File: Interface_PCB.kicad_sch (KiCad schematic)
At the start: 40 parts, among them IC1 STM32L412RBT6P, J1 USB_B, J2 AVR-JTAG-10, J3 Conn_01x04, J4 Conn_01x04, J5 Conn_01x04, J6 Conn_01x04, J7 Micro_SD_Card, U1 AMS1117-3.3, Y1 Crystal, Y2 Crystal

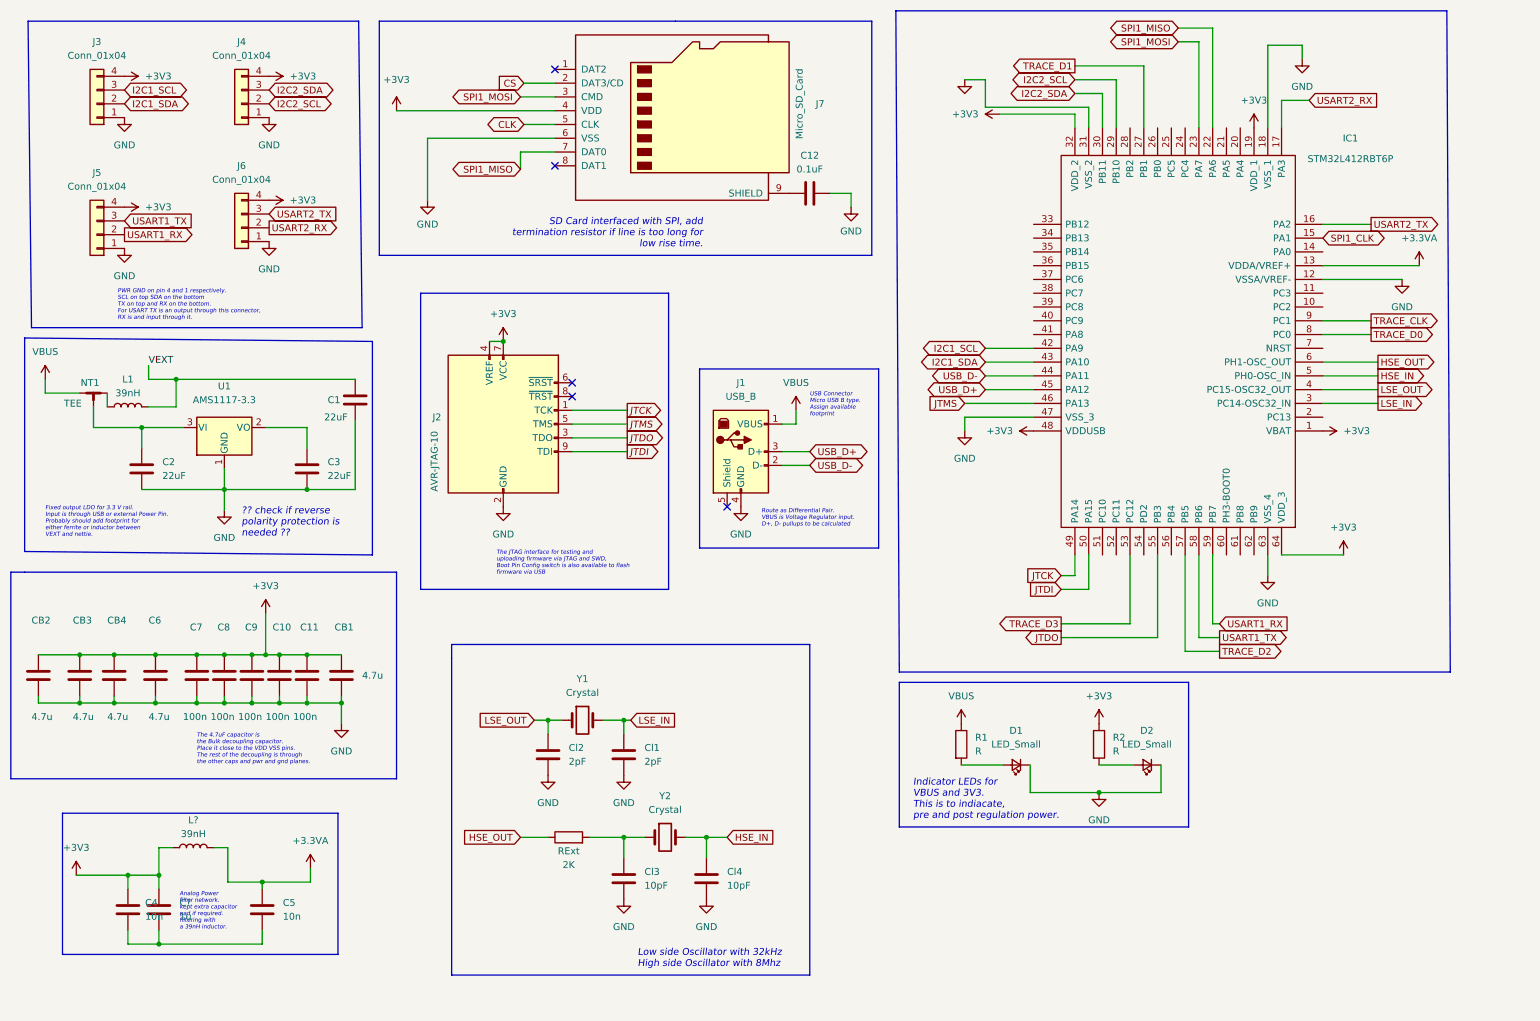
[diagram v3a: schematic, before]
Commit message: Components are on PCB doc, Stackup and Layout to be done, verify footprints
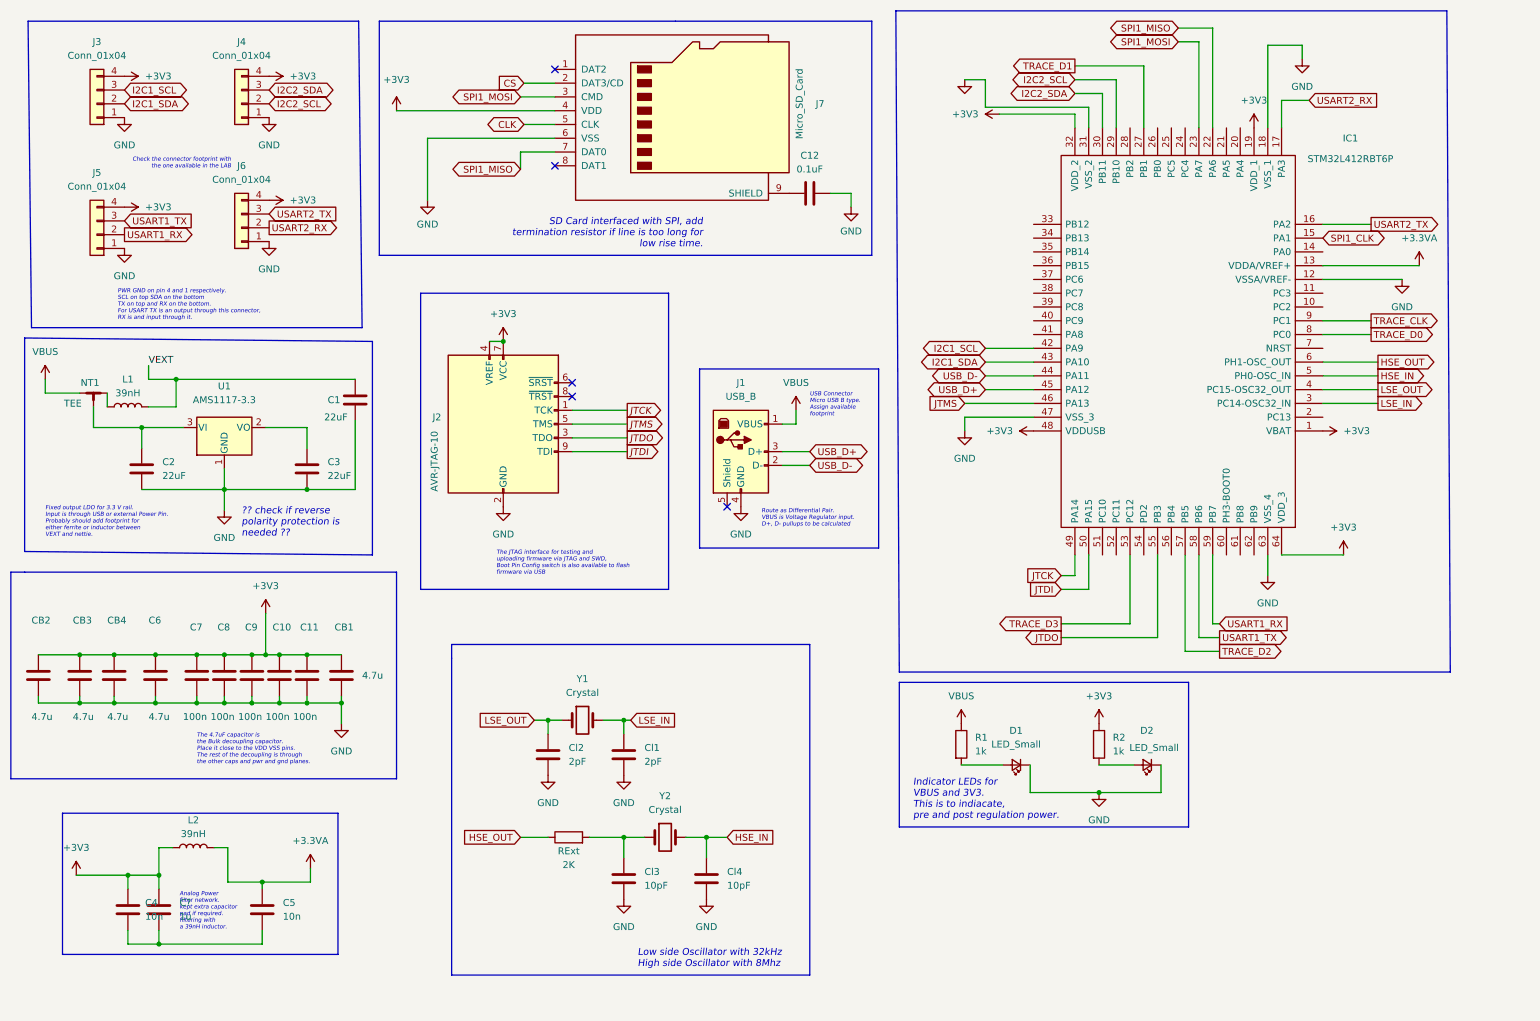
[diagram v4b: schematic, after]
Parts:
- C1, C10, C11, C2, C3, C4, C5, C7, C8, C9, C?: footprint (none) -> Capacitor_SMD:C_0603_1608Metric
- C6, CB1, CB2, CB3, CB4: footprint (none) -> Capacitor_SMD:C_0805_2012Metric
- Cl1, Cl2, Cl3, Cl4: footprint (none) -> Capacitor_SMD:C_0402_1005Metric
- D1, D2: footprint (none) -> LED_SMD:LED_0603_1608Metric
- J2: footprint (none) -> Connector_PinHeader_2.54mm:PinHeader_2x05_P2.54mm_Vertical_SMD
- J4, J5, J6: footprint (none) -> Connector_Molex:Molex_CLIK-Mate_502382-0270_1x02-1MP_P1.25mm_Vertical
- L2: renamed from L?; footprint (none) -> Capacitor_SMD:C_0603_1608Metric
- R1, R2: value R -> 1k; footprint (none) -> Resistor_SMD:R_0603_1608Metric
- RExt: footprint (none) -> Resistor_SMD:R_0603_1608Metric
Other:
- note added: "Check the connector footprint with the one available in the LAB"

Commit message: Added all component links and modified the footprints
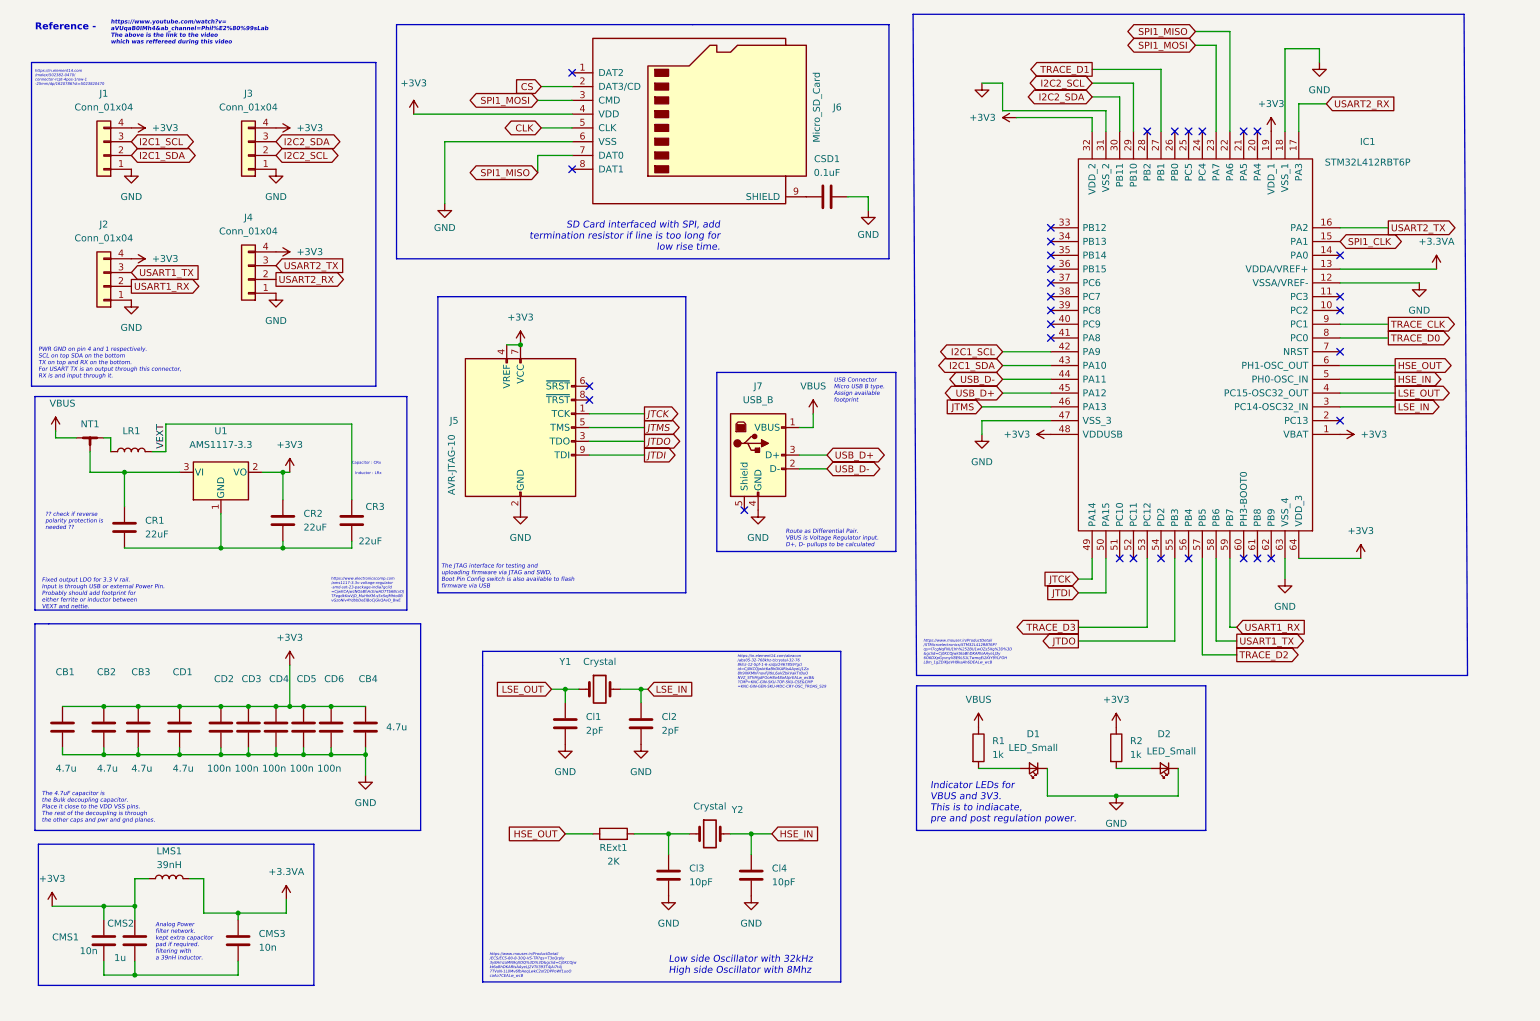
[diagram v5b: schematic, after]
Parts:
- removed C1, C2, C3: 22uF, Capacitor_SMD:C_0603_1608Metric, symbol Device:C
- removed C10, C11, C7, C8, C9: 100n, Capacitor_SMD:C_0603_1608Metric, symbol Device:C
- removed C12: 0.1uF, symbol Device:C
- removed C4, C5: 10n, Capacitor_SMD:C_0603_1608Metric, symbol Device:C
- removed C6: 4.7u, Capacitor_SMD:C_0805_2012Metric, symbol Device:C
- removed C?: 1u, Capacitor_SMD:C_0603_1608Metric, symbol Device:C
- removed J1: USB_B, Connector_USB:USB_Micro-B_Amphenol_10104110_Horizontal, symbol Connector:USB_B
- removed J2: AVR-JTAG-10, Connector_PinHeader_2.54mm:PinHeader_2x05_P2.54mm_Vertical_SMD, symbol Connector:AVR-JTAG-10
- removed J5, J6: Conn_01x04, Connector_Molex:Molex_CLIK-Mate_502382-0270_1x02-1MP_P1.25mm_Vertical, symbol Connector_Generic:Conn_01x04
- removed J7: Micro_SD_Card, Connector_Card:microSD_HC_Wuerth_693072010801, symbol Connector:Micro_SD_Card
- removed L1: 39nH, symbol Device:L
- removed L2: 39nH, Capacitor_SMD:C_0603_1608Metric, symbol Device:L
- removed RExt: 2K, Resistor_SMD:R_0603_1608Metric, symbol Device:R
- added CD1: 4.7u, Capacitor_SMD:C_0805_2012Metric, symbol Device:C
- added CD2, CD3, CD4, CD5, CD6: 100n, Capacitor_SMD:C_0603_1608Metric, symbol Device:C
- added CMS1, CMS3: 10n, Capacitor_SMD:C_0603_1608Metric, symbol Device:C
- added CMS2: 1u, Capacitor_SMD:C_0603_1608Metric, symbol Device:C
- added CR1, CR2, CR3: 22uF, Capacitor_SMD:C_0402_1005Metric, symbol Device:C
- added CSD1: 0.1uF, Capacitor_SMD:C_0402_1005Metric, symbol Device:C
- added J1, J2: Conn_01x04, Connector_Molex:Molex_CLIK-Mate_502382-0470_1x04-1MP_P1.25mm_Vertical, symbol Connector_Generic:Conn_01x04
- added J5: AVR-JTAG-10, Connector_PinHeader_2.54mm:PinHeader_2x05_P2.54mm_Vertical_SMD, symbol Connector:AVR-JTAG-10
- added J6: Micro_SD_Card, SamacSys_Parts:693072010801, symbol Connector:Micro_SD_Card
- added J7: USB_B, Connector_USB1:USB_Micro-B_Amphenol_10104110_Horizontal, symbol Connector:USB_B
- added LMS1: 39nH, Capacitor_SMD:C_0603_1608Metric, symbol Device:L
- added LR1: 39nH, Inductor_SMD:L_0402_1005Metric, symbol Device:L
- added RExt1: 2K, Resistor_SMD:R_0603_1608Metric, symbol Device:R
- J3: footprint (none) -> Connector_Molex:Molex_CLIK-Mate_502382-0470_1x04-1MP_P1.25mm_Vertical
- J4: footprint Connector_Molex:Molex_CLIK-Mate_502382-0270_1x02-1MP_P1.25mm_Vertical -> Connector_Molex:Molex_CLIK-Mate_502382-0470_1x04-1MP_P1.25mm_Vertical
- NT1: value TEE -> NetTie_3_Tee; footprint (none) -> NetTie:NetTie-3_SMD_Pad2.0mm
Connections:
- net +3.3VA: now also CMS3.1, LMS1.2
- net +3V3: now also U1.2 (VO), CD1.1, CD2.1, CD3.1, CD4.1, CD5.1, CD6.1, CMS1.1, CMS2.1, CR2.1, J1.4 (Pin_4), J2.4 (Pin_4), J5.4 (VREF), J5.7 (VCC), J6.4 (VDD), LMS1.1
- net CLK: now also J6.5 (CLK)
- net CS: now also J6.2 (DAT3/CD)
- net GND: now also CD1.2, CD2.2, CD3.2, CD4.2, CD5.2, CD6.2, CSD1.2, J1.1 (Pin_1), J2.1 (Pin_1), J5.10 (GND), J5.2 (GND), J6.6 (VSS), J7.4 (GND); no longer U1.1 (GND)
- net HSE_OUT: now also RExt1.1
- net I2C1_SCL: now also J1.3 (Pin_3); no longer J3.3 (Pin_3)
- net I2C1_SDA: now also J1.2 (Pin_2); no longer J3.2 (Pin_2)
- net I2C2_SCL: now also J3.2 (Pin_2); no longer J4.2 (Pin_2)
- net I2C2_SDA: now also J3.3 (Pin_3); no longer J4.3 (Pin_3)
- net JTCK: now also J5.1 (TCK)
- net JTDI: now also J5.9 (TDI)
- net JTDO: now also J5.3 (TDO)
- net JTMS: now also J5.5 (TMS)
- net LSE_IN: now also Cl2.1; no longer Cl1.1
- net LSE_OUT: now also Cl1.1; no longer Cl2.1
- net SPI1_MISO: now also J6.7 (DAT0)
- net SPI1_MOSI: now also J6.3 (CMD)
- net USART1_RX: now also J2.2 (Pin_2)
- net USART1_TX: now also J2.3 (Pin_3)
- net USART2_RX: now also J4.2 (Pin_2)
- net USART2_TX: now also J4.3 (Pin_3)
- net USB_D+: now also J7.3 (D+)
- net USB_D-: now also J7.2 (D-)
- net VBUS: now also J7.1 (VBUS)
- net VEXT: now also CR3.1, LR1.2
- net at Cl3.1, Y2.1: now also RExt1.2
- net at NT1.3, U1.3 (VI): now also CR1.1
- net at NT1.2: now also LR1.1
- new net: CR1.2, CR2.2, CR3.2, U1.1 (GND)
- new net: CMS1.2, CMS2.2, CMS3.2
- new net: CSD1.1, J6.9 (SHIELD)
- no-connect marks 5 -> 32
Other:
- note added: "Capacitor : CRx"
- note added: "Inductor : LRx"
- note added: "Reference -"
- note added: "https://in.element14.com /molex/502382-0470/ connector-rcpt-4pos-1row-1 -25mm/dp/1620786?st=5023820470"
- note added: "https://in.element14.com/abracon /abs05-32-768khz-t/crystal-32-76 8khz-12-5pf-1-6-x/dp/2467859?gcl id=Cj0KCQjwkt6aBhDKARIsAAyeLJ1Za 8h9IXKMhFnovFJltkL6aVZbkVakTrBuO NVZ_SThMgdFOoH8o48aAtprEALw_wcB& ?CMP=KNC-GIN-SKU-TOP-SKU-CSE&CMP =KNC-GIN-GEN-SKU-MDC-CRY-OSC_TROAS_S29"
- note added: "https://www.electronicscomp.com /ams1117-3.3v-voltage-regulator -smd-sot-23-package-india?gclid =CjwKCAjwzNOaBhAcEiwAD7Tb6BcvDJ TFegdkKwVjD_MuHhKM-s5xSejMhto0B vGzoNlv4YdbbDeElBoCjGkQAvD_BwE"
- note added: "https://www.mouser.in/ProductDetail /ECS/ECS-80-8-30Q-VS-TR?qs=T3oQrply 3y8AmzaMN9qXDQ%3D%3D&gclid=Cj0KCQjw kt6aBhDKARIsAAyeLJ2VTiI393T4jAi7t4j 7TVoN-1L0Mv6fbAeqLwkC2of2DPPoWf1uoO caAo7CEALw_wcB"
- note added: "https://www.mouser.in/ProductDetail /STMicroelectronics/STM32L412RBT6P? qs=l7cgNqFNU1hh%252BU1wOZs5Xg%3D%3D &gclid=Cj0KCQjwkt6aBhDKARIsAAyeLJ3y 6O6DXpGyvnyV8E9LS1LTwmqEi2KtY9YLFOH L8m_1gZDiKJeVH9kaAh6DEALw_wcB"
- note added: "https://www.youtube.com/watch?v= aVUqaB0IMh4&ab_channel=Phil%E2%80%99sLab The above is the link to the video which was reffereed during this video"
- note removed: "Check the connector footprint with the one available in the LAB"

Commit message: Layout Revision 1
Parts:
- added H1, H2, H3, H4: MountingHole, MountingHole:MountingHole_2.1mm, symbol Mechanical:MountingHole
- CD1: footprint Capacitor_SMD:C_0805_2012Metric -> Capacitor_SMD:C_0402_1005Metric
- CD2, CD3, CD4, CD5, CD6: footprint Capacitor_SMD:C_0603_1608Metric -> Capacitor_SMD:C_0402_1005Metric
- CMS1, CMS2, CMS3: footprint Capacitor_SMD:C_0603_1608Metric -> Capacitor_SMD:C_0805_2012Metric
- D1, D2: footprint LED_SMD:LED_0603_1608Metric -> LED_SMD:LED_0805_2012Metric
- J1, J2, J3, J4: footprint Connector_Molex:Molex_CLIK-Mate_502382-0470_1x04-1MP_P1.25mm_Vertical -> SamacSys_Parts:502382-0470
- J7: footprint Connector_USB1:USB_Micro-B_Amphenol_10104110_Horizontal -> SamacSys_Parts:GMCB05B11124H1EU
- R1, R2: footprint Resistor_SMD:R_0603_1608Metric -> Resistor_SMD:R_0805_2012Metric
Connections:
- net GND: now also CMS1.2, CMS2.2, CMS3.2, CR1.2, CR2.2, CR3.2, U1.1 (GND)
- net I2C2_SCL: now also J3.3 (Pin_3); no longer J3.2 (Pin_2)
- net I2C2_SDA: now also J3.2 (Pin_2); no longer J3.3 (Pin_3)

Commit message: Layout rev3.0 - redesigned
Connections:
- net CLK is gone; now on net SPI1_CLK: J6.5 (CLK)
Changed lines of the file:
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@@
     )
   )
-  (global_label "CLK" (shape bidirectional) (at 111.125 35.56 180) (fields_autoplaced)
+  (global_label "SPI1_CLK" (shape bidirectional) (at 111.125 35.56 180) (fields_autoplaced)
     (effects (font (size 1.27 1.27)) (justify right))
-    (property "Intersheet References" "${INTERSHEET_REFS}" (id 0) (at 105.1438 35.4806 0)
+    (property "Intersheet References" "${INTERSHEET_REFS}" (id 0) (at 99.8824 35.4806 0)
       (effects (font (size 1.27 1.27)) (justify right) hide)
     )

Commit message: Design rev4.0
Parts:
- J5: footprint Connector_PinHeader_2.54mm:PinHeader_2x05_P2.54mm_Vertical_SMD -> SamacSys_Parts:FTSH10501LDVK
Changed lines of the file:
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@@
       (effects (font (size 1.27 1.27)) (justify left))
     )
-    (property "Footprint" "MountingHole:MountingHole_2.1mm" (id 2) (at 271.78 138.43 0))
+    (property "Footprint" "MountingHole:MountingHole_2.1mm" (id 2) (at 266.7 140.97 0))
     (property "Datasheet" "~" (id 3) (at 271.78 144.78 0)
       (effects (font (size 1.27 1.27)) hide)
@@
       (effects (font (size 1.27 1.27)) (justify left))
     )
-    (property "Footprint" "MountingHole:MountingHole_2.1mm" (id 2) (at 273.05 153.67 0))
+    (property "Footprint" "MountingHole:MountingHole_2.1mm" (id 2) (at 266.7 154.94 0))
     (property "Datasheet" "~" (id 3) (at 273.05 160.02 0)
       (effects (font (size 1.27 1.27)) hide)
@@
       (effects (font (size 1.27 1.27)) (justify right))
     )
-    (property "Footprint" "Connector_PinHeader_2.54mm:PinHeader_2x05_P2.54mm_Vertical_SMD" (id 2) (at 103.505 86.995 90)
+    (property "Footprint" "SamacSys_Parts:FTSH10501LDVK" (id 2) (at 103.505 86.995 90)
       (effects (font (size 1.27 1.27)) hide)
     )
@@
     )
     (path "/6a7aa4a5-7205-48e3-98c3-381af2b97fa7"
-      (reference "J5") (unit 1) (value "AVR-JTAG-10") (footprint "Connector_PinHeader_2.54mm:PinHeader_2x05_P2.54mm_Vertical_SMD")
+      (reference "J5") (unit 1) (value "AVR-JTAG-10") (footprint "SamacSys_Parts:FTSH10501LDVK")
     )
     (path "/eca9c1d3-b80a-4529-b8b8-4a804ee1f35d"
